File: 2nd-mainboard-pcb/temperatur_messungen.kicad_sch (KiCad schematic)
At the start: 18 parts, among them J19 T2, J20 T2, J21 T2, J22 T3

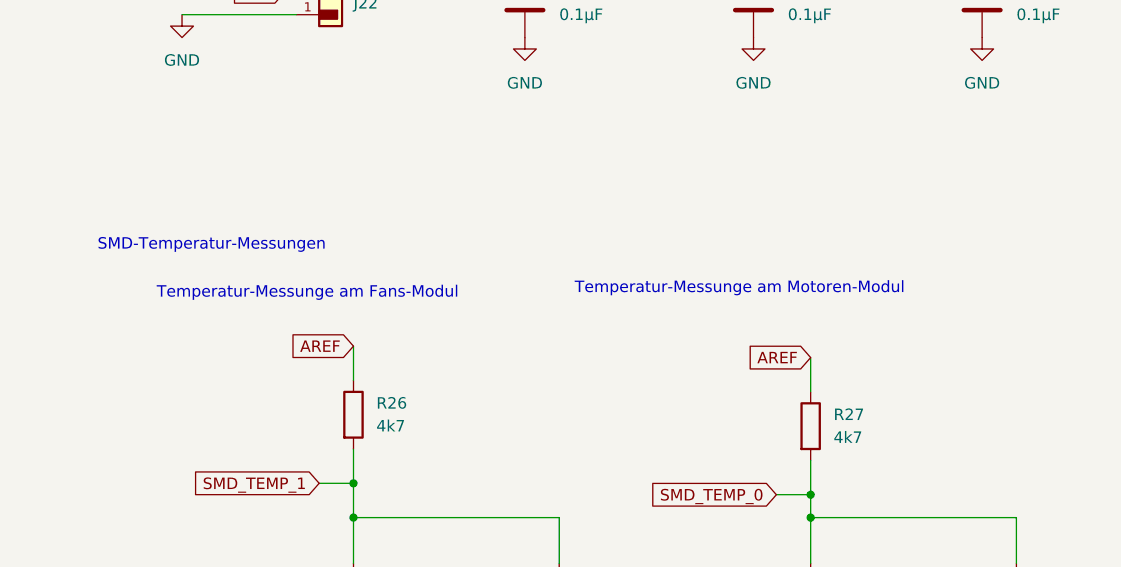
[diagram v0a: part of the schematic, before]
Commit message: pcb fans finished, pcb motors begin
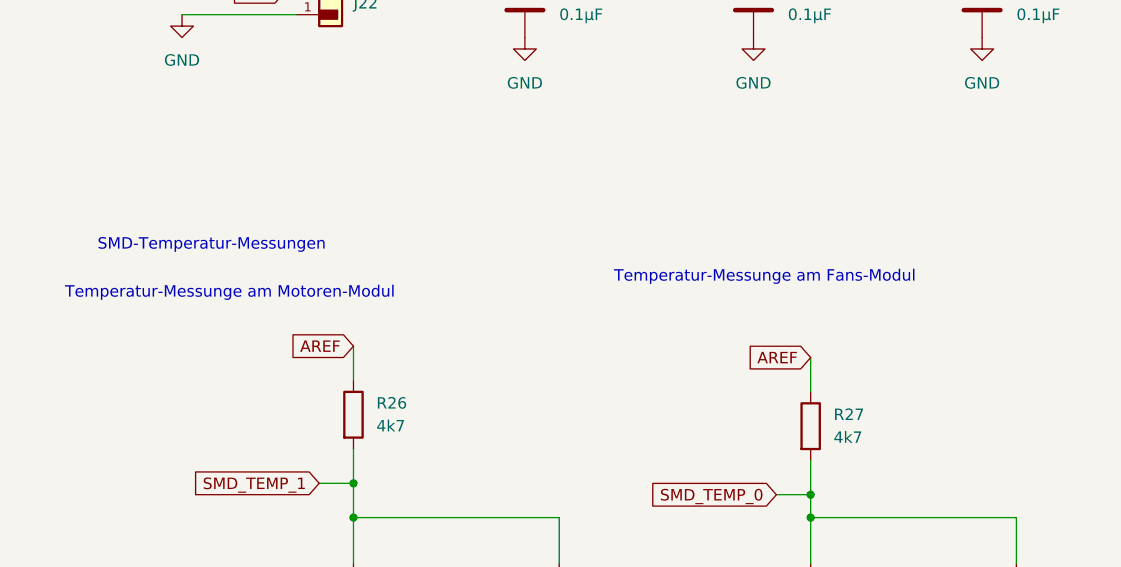
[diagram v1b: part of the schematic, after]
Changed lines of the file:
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@@
 	(text "Temperatur-Messunge am Fans-Modul"
 		(exclude_from_sim no)
-		(at 49.53 118.618 0)
+		(at 100.33 116.84 0)
 		(effects
 			(font
@@
 	(text "Temperatur-Messunge am Motoren-Modul"
 		(exclude_from_sim no)
-		(at 97.536 118.11 0)
+		(at 40.894 118.618 0)
 		(effects
 			(font

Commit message: Testpoints hinzugefügt
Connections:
- net +5V_POW renamed +5V_USBC
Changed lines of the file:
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@@
-	)
-	(symbol
-		(lib_id "power:+5VP")
-		(at 49.53 27.94 0)
-		(unit 1)
-		(exclude_from_sim no)
-		(in_bom yes)
-		(on_board yes)
-		(dnp no)
-		(fields_autoplaced yes)
-		(property "Reference" "#PWR0115"
-			(at 49.53 31.75 0)
-			(effects
-				(font
-					(size 1.27 1.27)
-				)
-				(hide yes)
-			)
-		)
-		(property "Value" "+5V_POW"
-			(at 49.53 22.86 0)
-			(effects
-				(font
-					(size 1.27 1.27)
-				)
-			)
-		)
-		(property "Footprint" ""
-			(at 49.53 27.94 0)
-			(effects
-				(font
-					(size 1.27 1.27)
-				)
-				(hide yes)
-			)
-		)
-		(property "Datasheet" ""
-			(at 49.53 27.94 0)
-			(effects
-				(font
-					(size 1.27 1.27)
-				)
-				(hide yes)
-			)
-		)
-		(property "Description" "Power symbol creates a global label with name \"+5VP\""
-			(at 49.53 27.94 0)
-			(effects
-				(font
-					(size 1.27 1.27)
-				)
-				(hide yes)
-			)
-		)
-		(pin "1"
-		)
-		(instances
-			(project "2nd-mainboard-pcb"
-				(path "/6926a609-8b92-4b3a-88c8-3d023174b977/2814f85c-0b7e-4ab3-b3e5-bcf29424baab/47263415-9ddd-4248-9320-66b73ee498aa"
-					(reference "#PWR0115")
-					(unit 1)
-				)
-			)
-		)
 	)
 	(symbol
@@
 					(unit 1)
 				)
+			)
+		)
+	)
+	(symbol
+		(lib_id "power:+5C")
+		(at 49.53 27.94 0)
+		(unit 1)
+		(exclude_from_sim no)
+		(in_bom yes)
+		(on_board yes)
+		(dnp no)
+		(property "Reference" "#PWR0115"
+			(at 49.53 31.75 0)
+			(effects
+				(font
+					(size 1.27 1.27)
+				)
+				(hide yes)
+			)
+		)
+		(property "Value" "+5V_USBC"
+			(at 49.5301 24.13 90)
+			(effects
+				(font
+					(size 1.27 1.27)
+				)
+				(justify left)
+			)
+		)
+		(property "Footprint" ""
+			(at 49.53 27.94 0)
+			(effects
+				(font
+					(size 1.27 1.27)
+				)
+				(hide yes)
+			)
+		)
+		(property "Datasheet" ""
+			(at 49.53 27.94 0)
+			(effects
+				(font
+					(size 1.27 1.27)
+				)
+				(hide yes)
+			)
+		)
+		(property "Description" "Power symbol creates a global label with name \"+5C\""
+			(at 49.53 27.94 0)
+			(effects
+				(font
+					(size 1.27 1.27)
+				)
+				(hide yes)
+			)
+		)
+		(pin "1"
+		)
+		(instances
+			(project "2nd-mainboard-pcb"
+				(path "/6926a609-8b92-4b3a-88c8-3d023174b977/2814f85c-0b7e-4ab3-b3e5-bcf29424baab/47263415-9ddd-4248-9320-66b73ee498aa"
+					(reference "#PWR0115")
+					(unit 1)
+				)

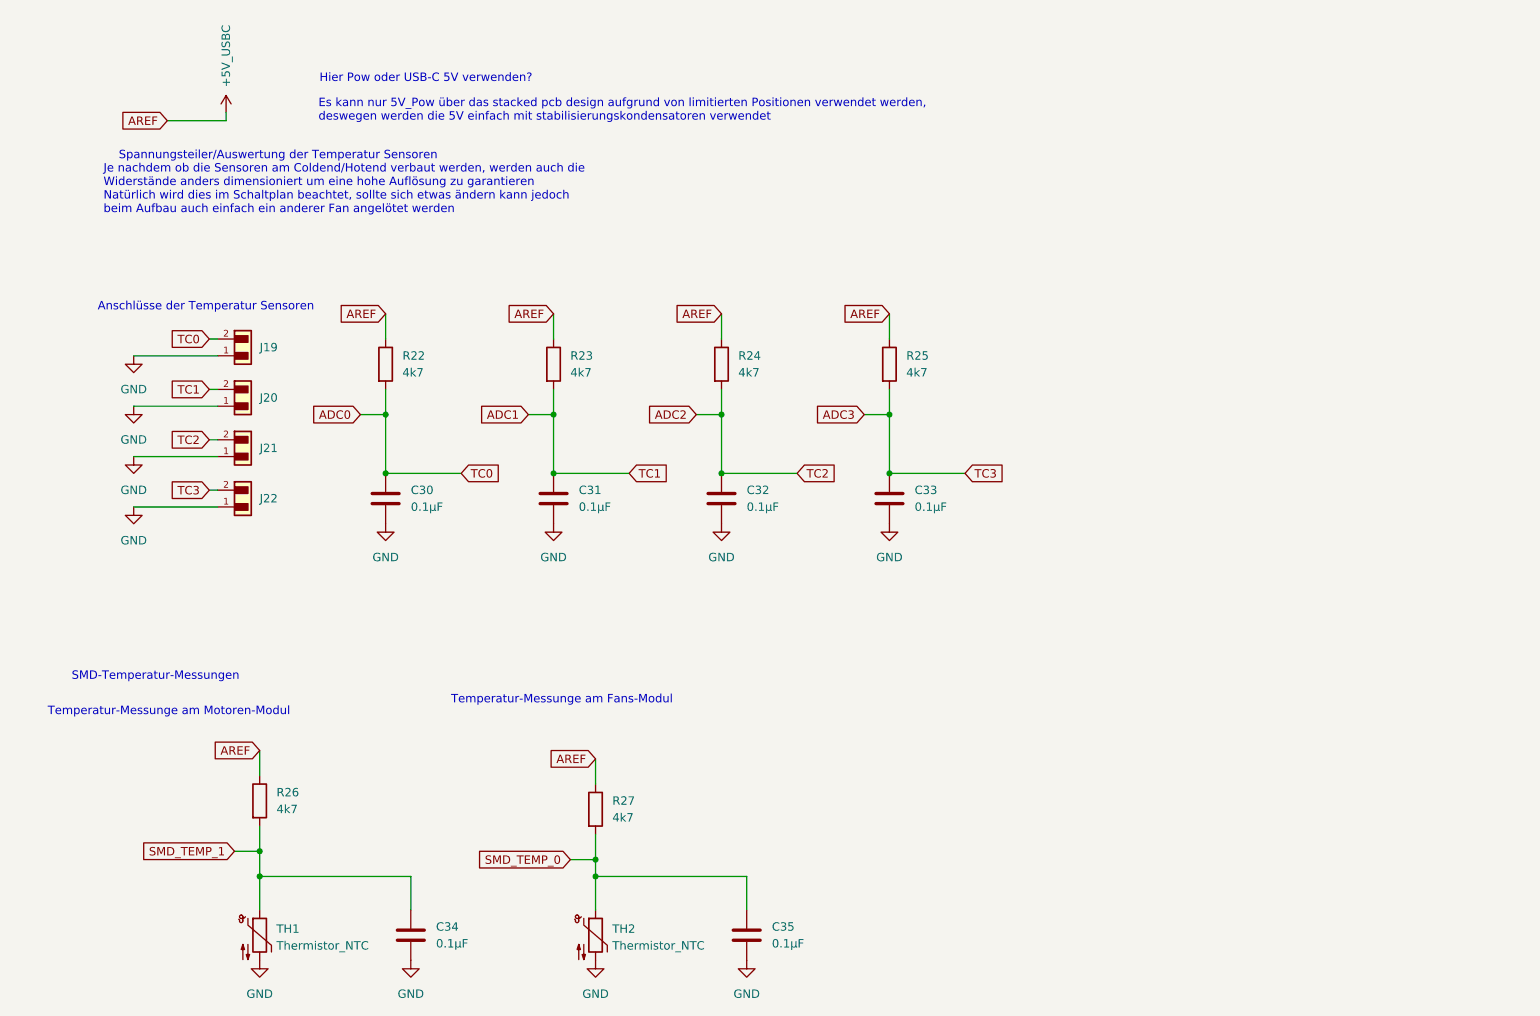
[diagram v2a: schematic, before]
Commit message: updated a bit of the track widths, removed comments in schematic
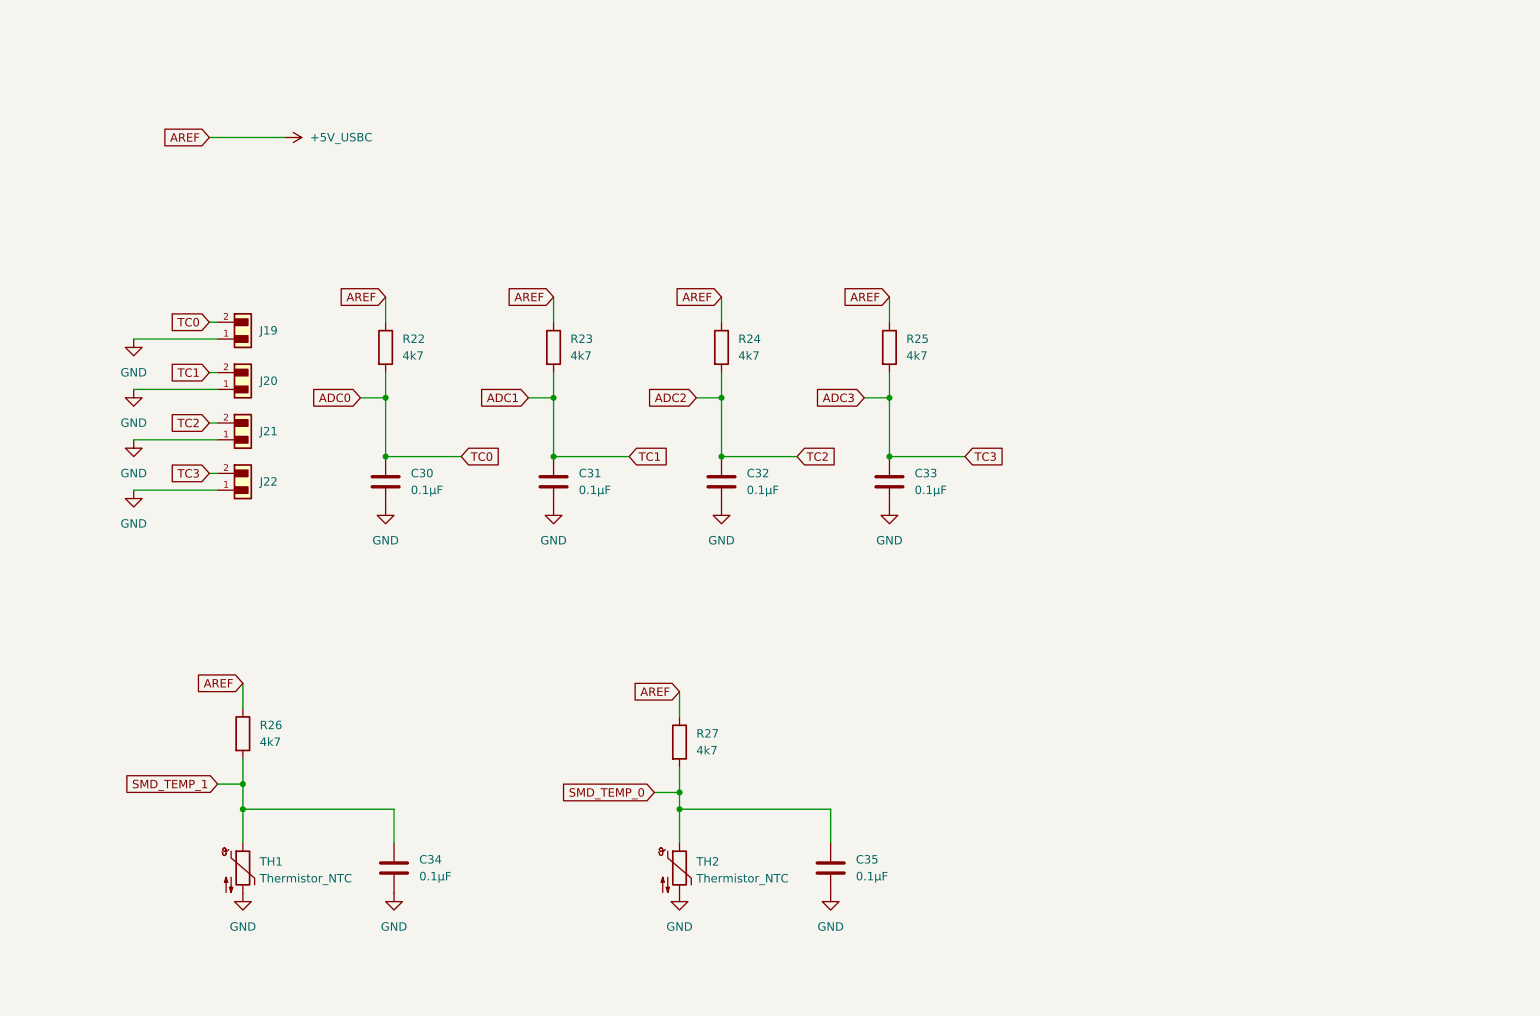
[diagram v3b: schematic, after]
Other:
- note removed: "Anschlüsse der Temperatur Sensoren"
- note removed: "Es kann nur 5V_Pow über das stacked pcb design aufgrund von limitierten Positionen verwendet werden, deswegen werden die 5V einfach mit stabilisierungskondensatoren verwendet"
- note removed: "Hier Pow oder USB-C 5V verwenden?"
- note removed: "Je nachdem ob die Sensoren am Coldend/Hotend verbaut werden, werden auch die Widerstände anders dimensioniert um eine hohe Auflösung zu garantieren Natürlich wird dies im Schaltplan beachtet, sollte sich etwas ändern kann jedoch beim Aufbau auch einfach ein anderer Fan angelötet werden"
- note removed: "SMD-Temperatur-Messungen"
- note removed: "Spannungsteiler/Auswertung der Temperatur Sensoren"
- note removed: "Temperatur-Messunge am Fans-Modul"
- note removed: "Temperatur-Messunge am Motoren-Modul"
- moved on the sheet: C30, C31, C32, C33, C34, C35, J19, J20, J21, J22, R22, R23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

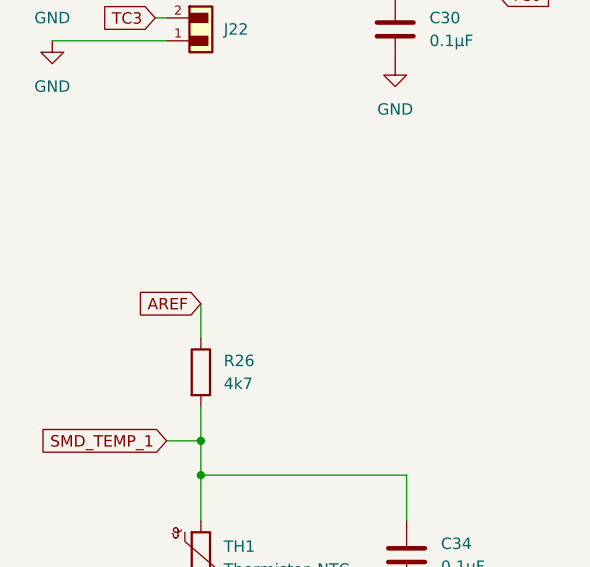
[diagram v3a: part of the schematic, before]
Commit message: DRC fehler behoben ca 200 stueck, jetzt gehts ans pcb ausschneiden
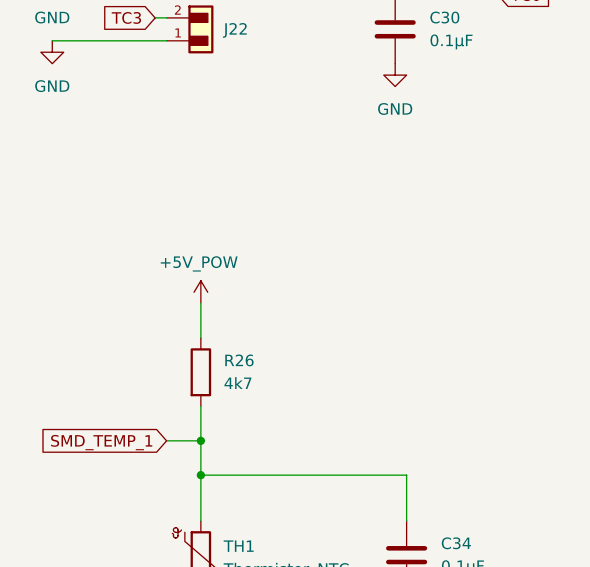
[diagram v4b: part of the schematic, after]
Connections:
- net +5V_USBC: no longer R26.1
- new net +5V_POW: R26.1
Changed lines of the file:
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@@
-	(global_label "AREF"
-		(shape input)
-		(at 52.07 114.3 180)
-		(fields_autoplaced yes)
-		(effects
-			(font
-				(size 1.27 1.27)
-			)
-			(justify right)
-		)
-		(property "Intersheetrefs" "${INTERSHEET_REFS}"
-			(at 44.4886 114.3 0)
-			(effects
-				(font
-					(size 1.27 1.27)
-				)
-				(justify right)
-				(hide yes)
-			)
-		)
-	)
 	(global_label "AREF"
 		(shape input)
@@
 					(unit 1)
 				)
+			)
+		)
+	)
+	(symbol
+		(lib_id "power:+5VP")
+		(at 52.07 114.3 0)
+		(unit 1)
+		(exclude_from_sim no)
+		(in_bom yes)
+		(on_board yes)
+		(dnp no)
+		(property "Reference" "#PWR095"
+			(at 52.07 118.11 0)
+			(effects
+				(font
+					(size 1.27 1.27)
+				)
+				(hide yes)
+			)
+		)
+		(property "Value" "+5V_POW"
+			(at 51.816 109.728 0)
+			(effects
+				(font
+					(size 1.27 1.27)
+				)
+			)
+		)
+		(property "Footprint" ""
+			(at 52.07 114.3 0)
+			(effects
+				(font
+					(size 1.27 1.27)
+				)
+				(hide yes)
+			)
+		)
+		(property "Datasheet" ""
+			(at 52.07 114.3 0)
+			(effects
+				(font
+					(size 1.27 1.27)
+				)
+				(hide yes)
+			)
+		)
+		(property "Description" "Power symbol creates a global label with name \"+5VP\""
+			(at 52.07 114.3 0)
+			(effects
+				(font
+					(size 1.27 1.27)
+				)
+				(hide yes)
+			)
+		)
+		(pin "1"
+		)
+		(instances
+			(project "2nd-mainboard-pcb"
+				(path "/6926a609-8b92-4b3a-88c8-3d023174b977/2814f85c-0b7e-4ab3-b3e5-bcf29424baab/47263415-9ddd-4248-9320-66b73ee498aa"
+					(reference "#PWR095")
+					(unit 1)
+				)

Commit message: stacked pcb reworked
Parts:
- removed C34, C35: 0.1µF, Capacitor_SMD:C_0402_1005Metric_Pad0.74x0.62mm_HandSolder, symbol Device:C
- removed R26, R27: 4k7, Resistor_SMD:R_0402_1005Metric, symbol Device:R
- removed TH1, TH2: Thermistor_NTC, Resistor_SMD:R_0805_2012Metric, symbol Device:Thermistor_NTC
- added C36: 10µF, Capacitor_SMD:C_0805_2012Metric_Pad1.18x1.45mm_HandSolder, symbol Device:C
- added C37: 100nF, Capacitor_SMD:C_0402_1005Metric_Pad0.74x0.62mm_HandSolder, symbol Device:C
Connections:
- net +5V_USBC: now also C36.1, C37.1
- net GND: now also C36.2, C37.2
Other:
- moved on the sheet: C30, C31, C32, C33, J19, J20, J21, J22, R22, R23, R24, R25

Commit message: rearragned componentens
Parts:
- C30, C31, C32, C33, C37: footprint Capacitor_SMD:C_0402_1005Metric_Pad0.74x0.62mm_HandSolder -> Capacitor_SMD:C_0603_1608Metric_Pad1.08x0.95mm_HandSolder
- R22, R23, R24, R25: footprint Resistor_SMD:R_0402_1005Metric -> Resistor_SMD:R_0603_1608Metric_Pad0.98x0.95mm_HandSolder
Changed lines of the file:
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@@
 			)
 		)
-		(property "Footprint" "Capacitor_SMD:C_0402_1005Metric_Pad0.74x0.62mm_HandSolder"
+		(property "Footprint" "Capacitor_SMD:C_0603_1608Metric_Pad1.08x0.95mm_HandSolder"
 			(at 136.8552 63.5 0)
 			(effects
@@
 			)
 		)
-		(property "Footprint" "Resistor_SMD:R_0402_1005Metric"
+		(property "Footprint" "Resistor_SMD:R_0603_1608Metric_Pad0.98x0.95mm_HandSolder"
 			(at 184.912 39.37 90)
 			(effects
@@
 			)
 		)
-		(property "Footprint" "Capacitor_SMD:C_0402_1005Metric_Pad0.74x0.62mm_HandSolder"
+		(property "Footprint" "Capacitor_SMD:C_0603_1608Metric_Pad1.08x0.95mm_HandSolder"
 			(at 111.4552 63.5 0)
 			(effects
@@
 			)
 		)
-		(property "Footprint" "Capacitor_SMD:C_0402_1005Metric_Pad0.74x0.62mm_HandSolder"
+		(property "Footprint" "Capacitor_SMD:C_0603_1608Metric_Pad1.08x0.95mm_HandSolder"
 			(at 187.6552 63.5 0)
 			(effects
@@
 			)
 		)
-		(property "Footprint" "Resistor_SMD:R_0402_1005Metric"
+		(property "Footprint" "Resistor_SMD:R_0603_1608Metric_Pad0.98x0.95mm_HandSolder"
 			(at 108.712 39.37 90)
 			(effects
@@
 			)
 		)
-		(property "Footprint" "Capacitor_SMD:C_0402_1005Metric_Pad0.74x0.62mm_HandSolder"
+		(property "Footprint" "Capacitor_SMD:C_0603_1608Metric_Pad1.08x0.95mm_HandSolder"
 			(at 53.0352 40.64 0)
 			(effects
@@
 			)
 		)
-		(property "Footprint" "Capacitor_SMD:C_0402_1005Metric_Pad0.74x0.62mm_HandSolder"
+		(property "Footprint" "Capacitor_SMD:C_0603_1608Metric_Pad1.08x0.95mm_HandSolder"
 			(at 162.2552 63.5 0)
 			(effects
@@
 			)
 		)
-		(property "Footprint" "Resistor_SMD:R_0402_1005Metric"
+		(property "Footprint" "Resistor_SMD:R_0603_1608Metric_Pad0.98x0.95mm_HandSolder"
 			(at 159.512 39.37 90)
 			(effects
@@
 			)
 		)
-		(property "Footprint" "Resistor_SMD:R_0402_1005Metric"
+		(property "Footprint" "Resistor_SMD:R_0603_1608Metric_Pad0.98x0.95mm_HandSolder"
 			(at 134.112 39.37 90)
 			(effects
